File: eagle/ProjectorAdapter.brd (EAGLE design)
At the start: 18 x 21 mm, 8 parts, among them J1 0532610271, J3 0532610471, J4 0532610271

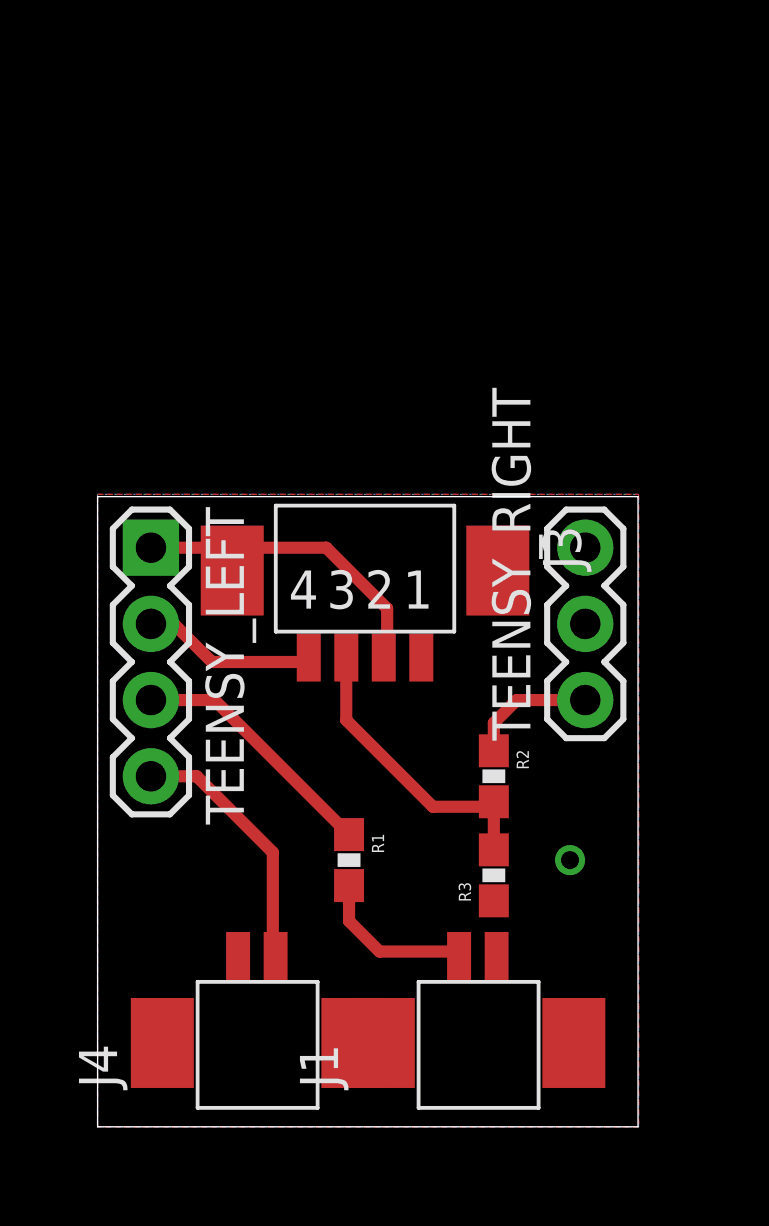
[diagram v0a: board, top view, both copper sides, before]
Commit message: updated pcb with molex connectors; created 6 pin connector. updated code for different pin definitions.
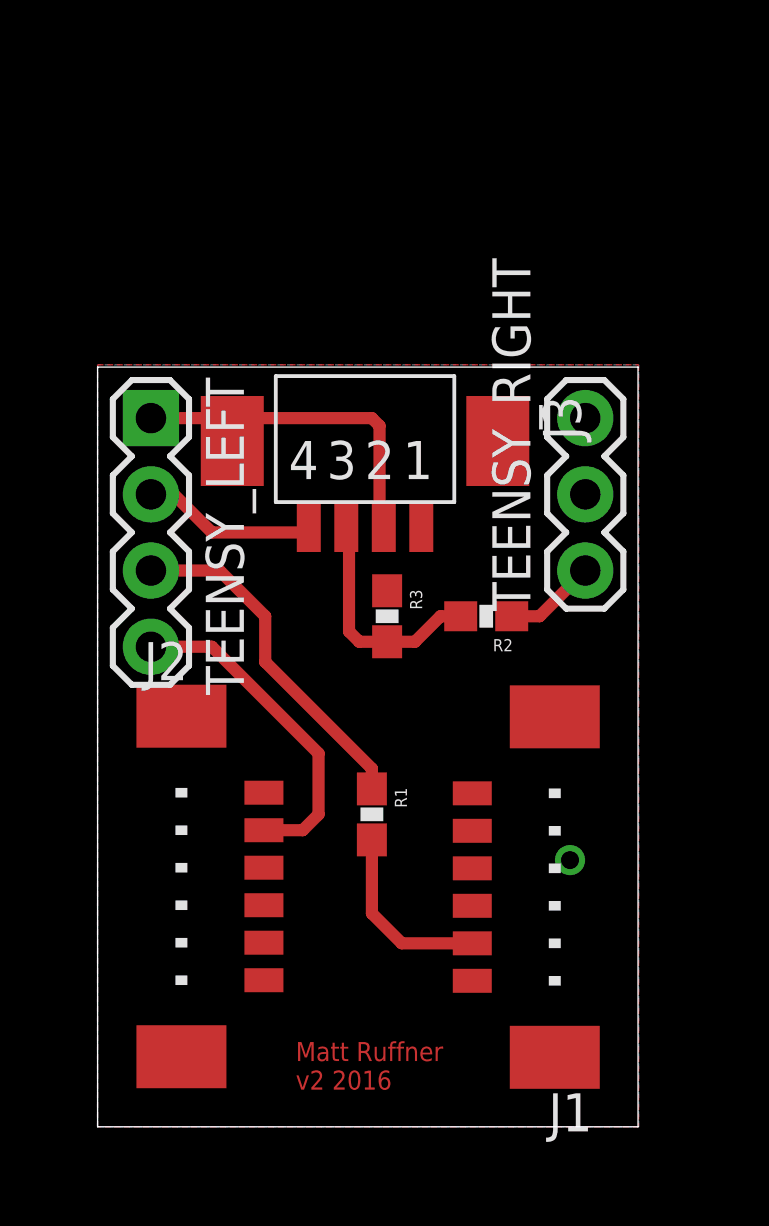
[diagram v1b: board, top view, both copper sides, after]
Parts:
- removed J4: 0532610271, volks73-Molex:PICOBLADE53261-0271
- added J2: 05339805711, volks73-Molex:PICOBLADE53398-0671
- J1: value 0532610271 -> 05339805711; device volks73-Molex:PICOBLADE53261-0271 -> volks73-Molex:PICOBLADE53398-0671
- moved R3 9.34 mm to (9.65, 17.0), turned to 270 degrees
- moved R2 5.34 mm to (13.0, 17.0), turned to 180 degrees
- moved J1 5.23 mm to (15.2, 7.37), turned to 90 degrees
- moved TEENSY_LEFT 4.32 mm to (1.78, 23.6)
- moved TEENSY_RIGHT 4.32 mm to (16.3, 18.5)
- moved J3 4.32 mm to (8.89, 22.9)
- moved R1 1.70 mm to (9.14, 10.4)
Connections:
- net FROM_PROJ: now also J2.2; no longer J4.1
- net GND: now also J1.3, J2.3; no longer J1.1, J4.2
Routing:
- net TO_PROJ: track 8.46 -> 11.7 mm
- net FROM_PROJ: track 8.60 -> 11.1 mm
- net N$2: track 9.87 -> 7.70 mm
- net 3V3: track 4.29 -> 3.08 mm
- net N$4: track 5.33 -> 6.21 mm
- net GND: track 10.4 -> 11.2 mm
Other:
- board size 18 x 21 mm -> 18 x 25.3 mm
- board text added: "Matt Ruffner v2 2016"

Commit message: designed rev3 board to cover full teensy bottom and mount below it.
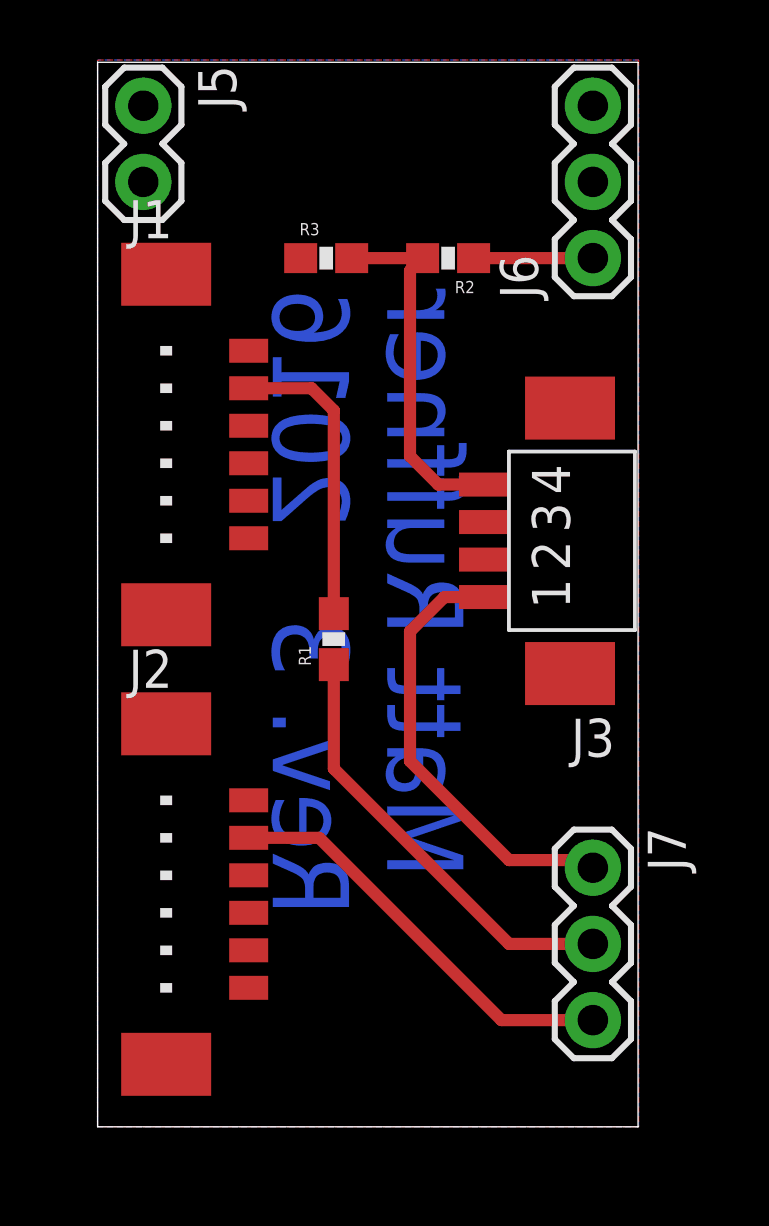
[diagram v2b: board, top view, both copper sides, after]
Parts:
- removed TEENSY_LEFT: (no value), SparkFun-Connectors:1X04
- removed TEENSY_RIGHT: (no value), SparkFun-Connectors:1X03
- added J5: (no value), SparkFun-Connectors:1X02
- added J6, J7: (no value), SparkFun-Connectors:1X03
- moved J1 20.6 mm to (2.29, 23.4), turned to 270 degrees
- moved R3 12.1 mm to (7.62, 29.0), turned to 0 degrees
- moved R2 12.0 mm to (11.7, 29.0)
- moved J3 7.61 mm to (15.7, 19.6), turned to 90 degrees
- moved R1 5.98 mm to (7.87, 16.3), turned to 90 degrees
- moved J2 0.57 mm to (2.29, 8.38)
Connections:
- net 3V3: now also J6.1; no longer TEENSY_RIGHT.1
- net FROM_PROJ: now also J7.3; no longer TEENSY_LEFT.4
- net GND: now also J3.3, J5.1; no longer J3.1, TEENSY_LEFT.1
- net N$2: now also J3.4; no longer J3.3
- net TO_CAMERA: now also J3.1, J7.1; no longer J3.4, TEENSY_LEFT.2
- net TO_PROJ: now also J7.2; no longer TEENSY_LEFT.3
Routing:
- net GND: track 11.2 -> 0.00 mm, vias 1 -> 0
- net TO_CAMERA: track 5.85 -> 14.8 mm
- net N$2: track 7.70 -> 12.0 mm
- net N$4: track 6.21 -> 9.92 mm
- net FROM_PROJ: track 11.1 -> 14.0 mm
- net TO_PROJ: track 11.7 -> 14.5 mm
- net 3V3: track 3.08 -> 3.98 mm
- added copper zone on layer 16, net N$10
- removed copper zone on layer 16, net GND
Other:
- board size 18 x 25.3 mm -> 18 x 35.5 mm
- board text added: "Matt Ruffner Rev. 3 2016"
- board text removed: "Matt Ruffner v2 2016"

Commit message: added old silk changes
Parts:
- moved J3 14.8 mm to (9.14, 32.8), flipped to the bottom, turned to 180 degrees
- moved R3 6.91 mm to (13.2, 24.9), flipped to the bottom
- moved R2 2.34 mm to (13.2, 27.2), flipped to the bottom, turned to 0 degrees
- moved J1 1.30 mm to (2.54, 22.1), flipped to the bottom, turned to 90 degrees
- moved J2 1.30 mm to (2.54, 7.11), flipped to the bottom, turned to 90 degrees
- flipped R1 to the bottom
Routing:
- net TO_CAMERA: track 14.8 -> 27.8 mm
- net N$2: track 12.0 -> 5.54 mm
- net N$4: track 9.92 -> 5.87 mm
- net FROM_PROJ: track 14.0 -> 12.2 mm
- net 3V3: track 3.98 -> 3.19 mm
- net TO_PROJ: track 14.5 -> 15.3 mm
- added copper zone on layer 16, net GND
- removed copper zone on layer 16, net N$10
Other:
- board text removed: "Matt Ruffner Rev. 3 2016"
